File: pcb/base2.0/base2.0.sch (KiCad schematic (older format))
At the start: 32 parts, among them J1 Conn_01x01_Male, J2 Conn_01x01_Male, J3 Conn_01x04_Male, J4 Conn_01x02_Male, U1 STM32G431CBU6, U2 tile, U3 AP2210-33, U4 MPU-9250

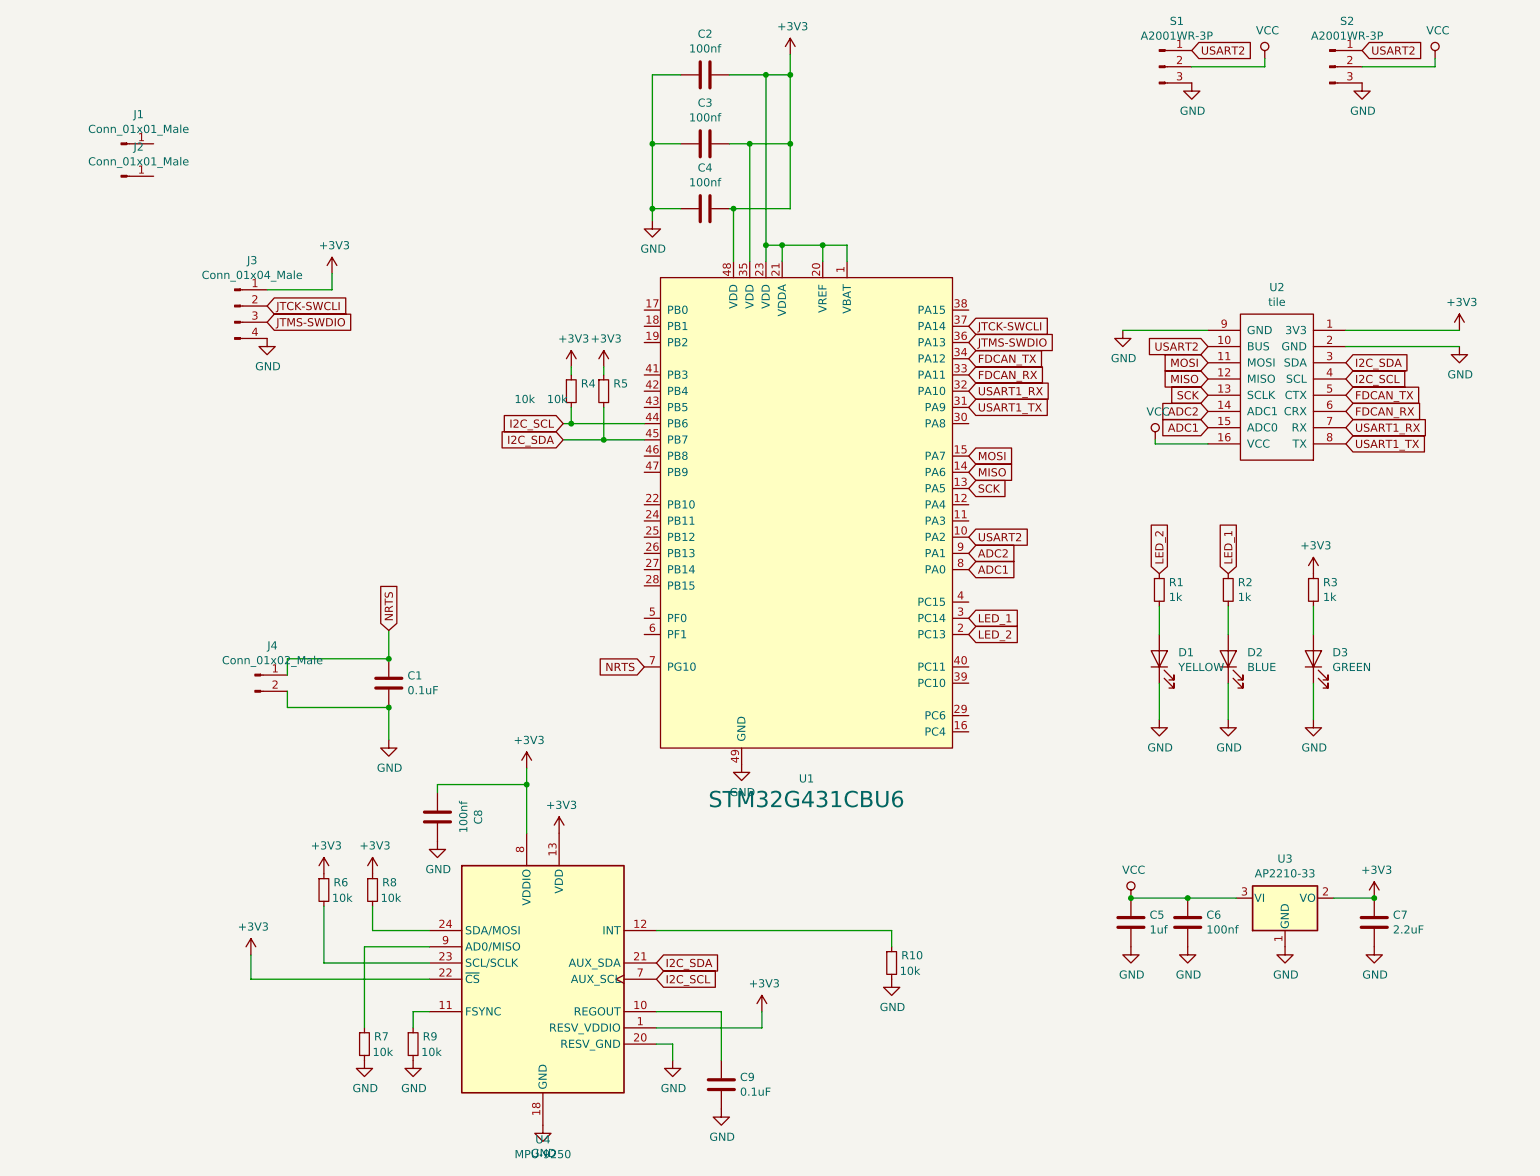
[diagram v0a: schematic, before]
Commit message: fixed errors in scheme
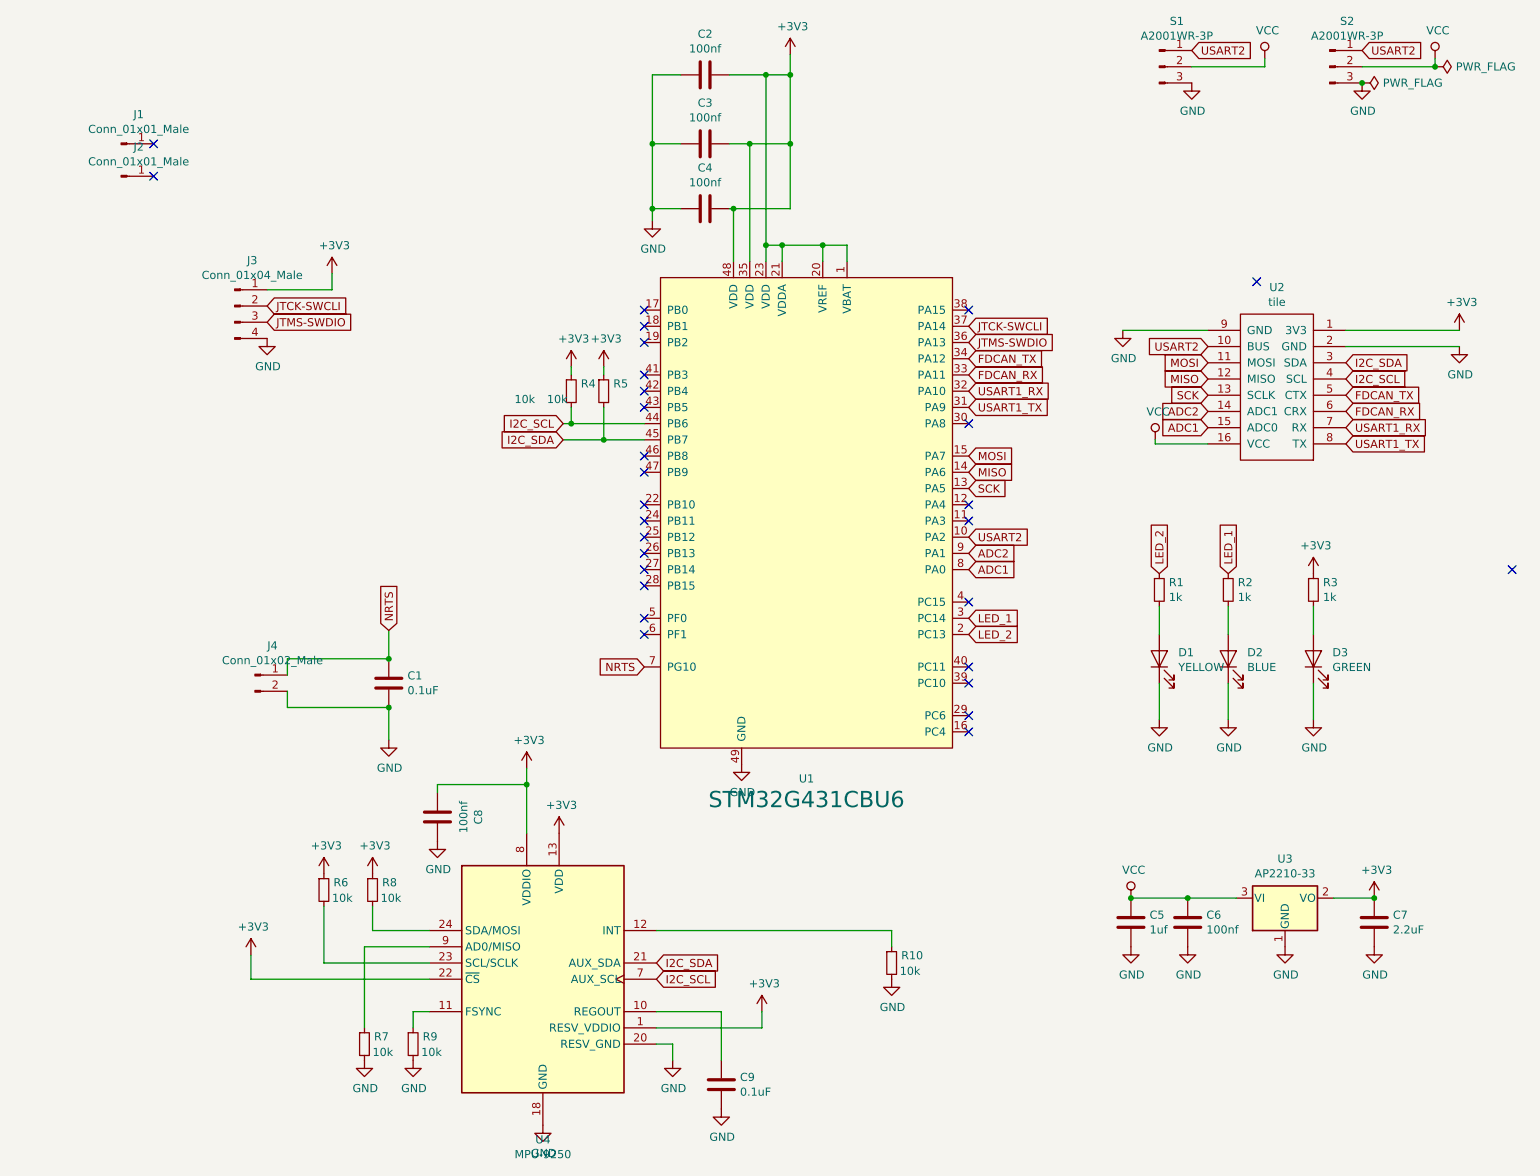
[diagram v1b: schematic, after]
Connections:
- no-connect marks 0 -> 29
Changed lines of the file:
@@
 Wire Wire Line
 	2400 2250 2400 2150
+$Comp
+L power:PWR_FLAG #FLG0101
+U 1 1 602FFDF2
+P 8750 975
+F 0 "#FLG0101" H 8750 1050 50  0001 C CNN
+F 1 "PWR_FLAG" V 8750 1103 50  0000 L CNN
+F 2 "" H 8750 975 50  0001 C CNN
+F 3 "~" H 8750 975 50  0001 C CNN
+	1    8750 975
+	0    1    1    0
+$EndComp
+$Comp
+L power:PWR_FLAG #FLG0102
+U 1 1 60300624
+P 9200 875
+F 0 "#FLG0102" H 9200 950 50  0001 C CNN
+F 1 "PWR_FLAG" V 9200 1003 50  0000 L CNN
+F 2 "" H 9200 875 50  0001 C CNN
+F 3 "~" H 9200 875 50  0001 C CNN
+	1    9200 875
+	0    1    1    0
+$EndComp
+Connection ~ 9200 875
+Connection ~ 8750 975
+NoConn ~ 4325 2375
+NoConn ~ 4325 2475
+NoConn ~ 4325 2575
+NoConn ~ 4325 2775
+NoConn ~ 4325 2875
+NoConn ~ 4325 2975
+NoConn ~ 4325 3275
+NoConn ~ 4325 3375
+NoConn ~ 4325 3575
+NoConn ~ 4325 3675
+NoConn ~ 4325 3775
+NoConn ~ 4325 3875
+NoConn ~ 4325 3975
+NoConn ~ 4325 4075
+NoConn ~ 4325 4275
+NoConn ~ 4325 4375
+NoConn ~ 6325 4975
+NoConn ~ 6325 4875
+NoConn ~ 6325 4675
+NoConn ~ 6325 4575
+NoConn ~ 6325 4175
+NoConn ~ 6325 3675
+NoConn ~ 6325 3575
+NoConn ~ 6325 3075
+NoConn ~ 6325 2375
+NoConn ~ 9675 3975
+NoConn ~ 8100 2200
+NoConn ~ 1300 1350
+NoConn ~ 1300 1550
 $EndSCHEMATC

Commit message: le update
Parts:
- removed R10, R6, R7, R8, R9: 10k, Resistor_SMD:R_0402_1005Metric, symbol Device:R_Small
- removed U4: MPU-9250, Sensor_Motion:InvenSense_QFN-24_3x3mm_P0.4mm, symbol Sensor_Motion:MPU-9250
- added U4: LSM6DS3, Package_LGA:LGA-14_3x2.5mm_P0.5mm_LayoutBorder3x4y, symbol Sensor_Motion:LSM6DS3
- C9: value 0.1uF -> 100nf
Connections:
- net +3V3: now also C8.1, C9.2, U4.12 (CS), U4.5 (VDDIO), U4.8 (VDD); no longer C8.2
- net GND: now also C8.2, C9.1, U4.1 (SDO/SA0), U4.2 (SDX), U4.3 (SCX), U4.6 (GND), U4.7 (GND); no longer C8.1, C9.2
- net I2C_SCL: now also U4.13 (SCL)
- net I2C_SDA: now also U4.14 (SDA)

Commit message: Small changes to base pcb
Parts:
- removed J3: Conn_01x04_Male, Connector_PinHeader_2.00mm:PinHeader_1x04_P2.00mm_Vertical, symbol Connector:Conn_01x04_Male
- added C10: 1uf, Capacitor_SMD:C_0402_1005Metric, symbol Device:C
- added C11: 2.2uF, Capacitor_SMD:C_0402_1005Metric, symbol Device:C
- added J3: Conn_ARM_JTAG_SWD_10, Connector_PinHeader_1.27mm:PinHeader_2x05_P1.27mm_Vertical, symbol Connector:Conn_ARM_JTAG_SWD_10
- added Q1: BSS123, Package_TO_SOT_SMD:SOT-23, symbol Transistor_FET:BSS123
- added R6, R7: 10k, Resistor_SMD:R_0402_1005Metric, symbol Device:R_Small
- added U5: AP2210-5, Package_TO_SOT_SMD:SOT-23, symbol Regulator_Linear:AP1117-33
- S1, S2: footprint Connector_JST:JST_PH_S3B-PH-K_1x03_P2.00mm_Horizontal -> tile:jst_bus_horizontal
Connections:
- net +3V3: now also J3.1 (VTref), Q1.1 (G), R7.1
- net GND: now also S1.1 (Pin_1), S2.1 (Pin_1), C10.2, C11.2, J3.3 (GND), J3.5 (GND), J3.9 (GNDDetect), U5.1 (GND); no longer S1.3 (Pin_3), S2.3 (Pin_3)
- net I2C_SCL: now also U1.46 (PB8); no longer U1.44 (PB6)
- net JTCK-SWCLI: now also J3.4 (SWDCLK/TCK)
- net JTMS-SWDIO: now also J3.2 (SWDIO/TMS)
- net VCC: now also C10.1, U5.3 (VI)
- net USART2_RX: now reaches U1.11 (PA3)
- net USART2_RX: now also U2.7 (RX)
- net USART1_RX: no longer names the net of U1.32 (PA10)
- net USART1_RX: no longer U2.7 (RX)
- net USART1_TX renamed USART1_3
- net USART1_3: now also U2.10 (BUS), Q1.2 (S), R7.2; no longer U2.8 (TX)
- removed net USART2: S1.1 (Pin_1), S2.1 (Pin_1), U1.10 (PA2), U2.10 (BUS)
- new net +5V: C11.1, R6.1, U5.2 (VO)
- new net USART1_5: Q1.3 (D), R6.2, S1.3 (Pin_3), S2.3 (Pin_3)
- new net USART2_TX: U1.10 (PA2), U2.8 (TX)
- no-connect marks 29 -> 28
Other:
- moved on the sheet: R4
